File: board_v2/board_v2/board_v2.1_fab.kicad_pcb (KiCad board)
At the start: 2 copper layers, 55 x 61.5 mm, 38 parts, among them J1 Battery, J2 MOTR_SENS, J3 MOTL_SENS, J4 MOTL, J6 MOTR, SW1 SW_SPDT, U1 LD33V, U2 MPU-6050-Breakout, U3 DRV8313PWP, U5 DRV8313PWP

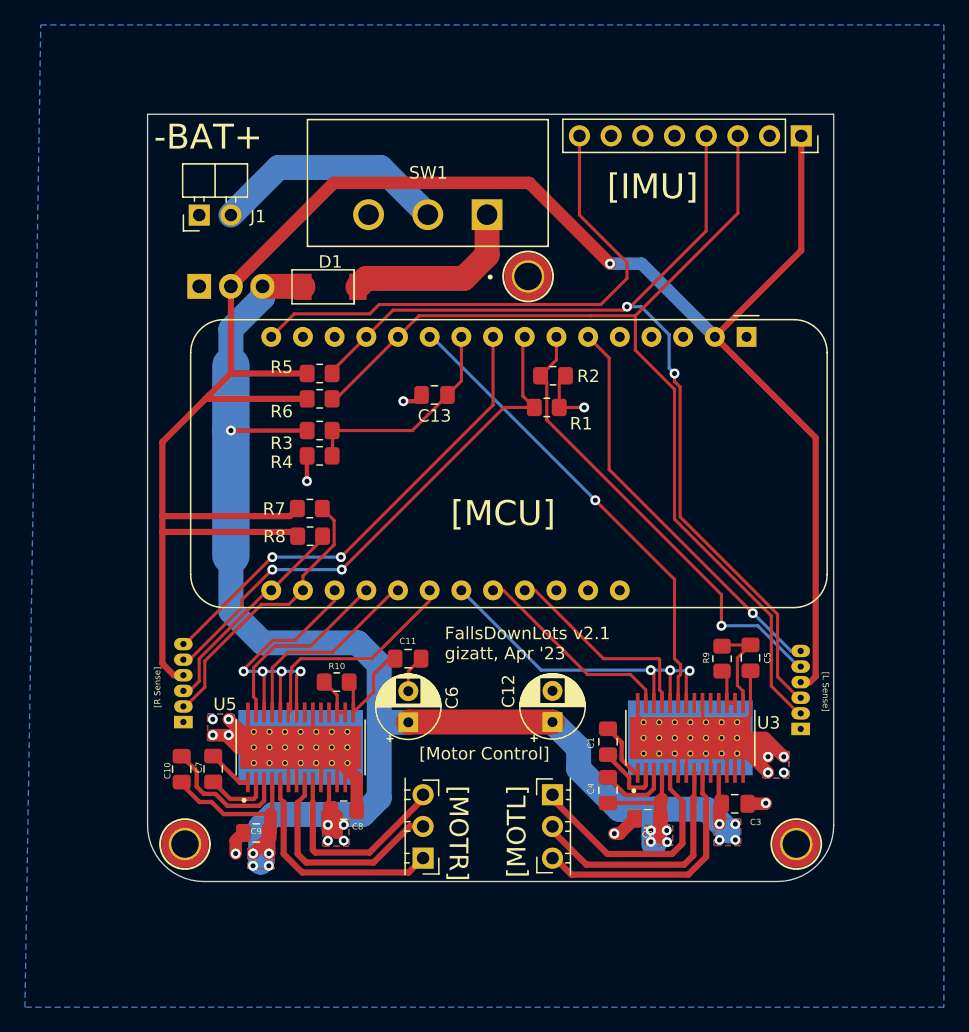
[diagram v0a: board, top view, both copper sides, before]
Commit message: Update V2 board schematics
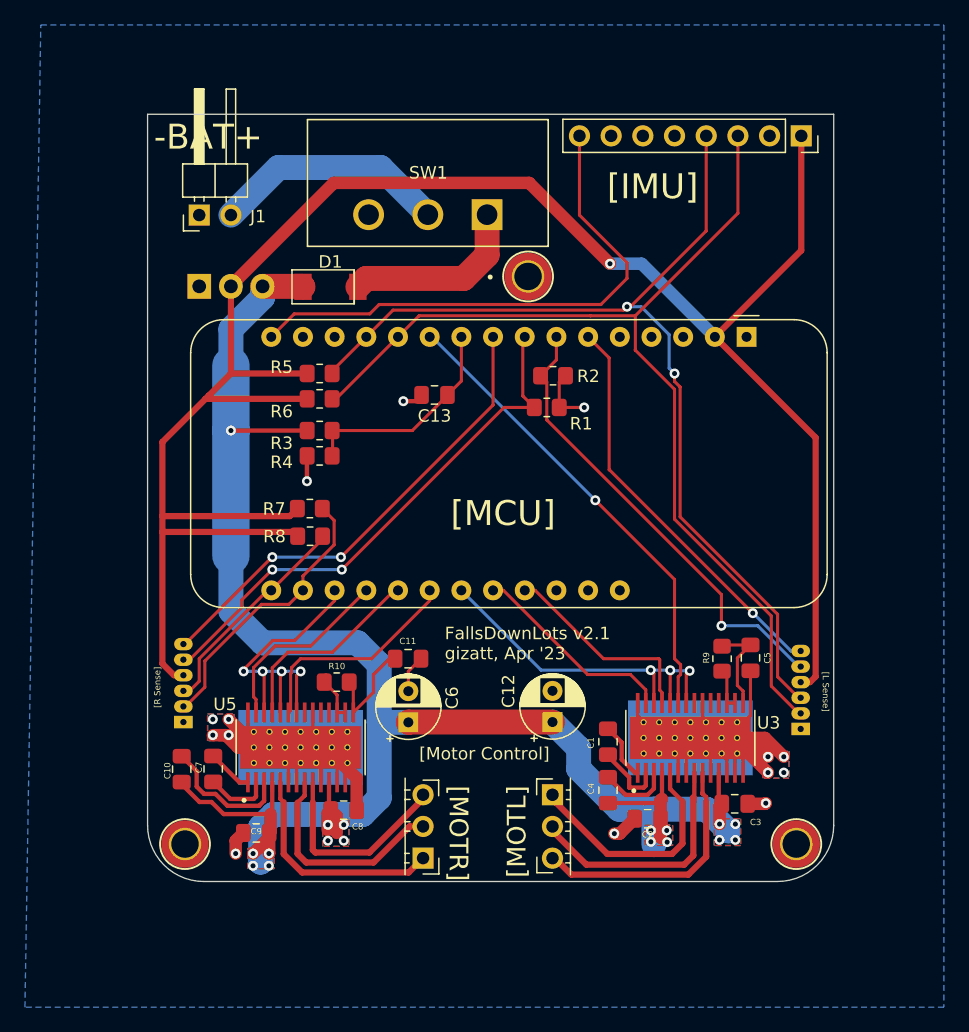
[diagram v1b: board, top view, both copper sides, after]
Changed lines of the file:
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@@
       (drillshape 0)
       (scaleselection 1)
-      (outputdirectory "v2.1_fab")
+      (outputdirectory "v2_fab")
     )
   )
@@
     (fp_line (start 4.1 -1.33) (end 1.44 -1.33)
       (stroke (width 0.12) (type solid)) (layer "F.SilkS"))
+    (fp_line (start 4.1 -0.38) (end 10.1 -0.38)
+      (stroke (width 0.12) (type solid)) (layer "F.SilkS"))
+    (fp_line (start 4.1 -0.32) (end 10.1 -0.32)
+      (stroke (width 0.12) (type solid)) (layer "F.SilkS"))
+    (fp_line (start 4.1 -0.2) (end 10.1 -0.2)
+      (stroke (width 0.12) (type solid)) (layer "F.SilkS"))
+    (fp_line (start 4.1 -0.08) (end 10.1 -0.08)
+      (stroke (width 0.12) (type solid)) (layer "F.SilkS"))
+    (fp_line (start 4.1 0.04) (end 10.1 0.04)
+      (stroke (width 0.12) (type solid)) (layer "F.SilkS"))
+    (fp_line (start 4.1 0.16) (end 10.1 0.16)
+      (stroke (width 0.12) (type solid)) (layer "F.SilkS"))
+    (fp_line (start 4.1 0.28) (end 10.1 0.28)
+      (stroke (width 0.12) (type solid)) (layer "F.SilkS"))
+    (fp_line (start 4.1 2.16) (end 10.1 2.16)
+      (stroke (width 0.12) (type solid)) (layer "F.SilkS"))
     (fp_line (start 4.1 3.87) (end 4.1 -1.33)
       (stroke (width 0.12) (type solid)) (layer "F.SilkS"))
+    (fp_line (start 10.1 -0.38) (end 10.1 0.38)
+      (stroke (width 0.12) (type solid)) (layer "F.SilkS"))
+    (fp_line (start 10.1 0.38) (end 4.1 0.38)
+      (stroke (width 0.12) (type solid)) (layer "F.SilkS"))
+    (fp_line (start 10.1 2.16) (end 10.1 2.92)
+      (stroke (width 0.12) (type solid)) (layer "F.SilkS"))
+    (fp_line (start 10.1 2.92) (end 4.1 2.92)
+      (stroke (width 0.12) (type solid)) (layer "F.SilkS"))
     (fp_line (start -1.8 -1.8) (end -1.8 4.35)
       (stroke (width 0.05) (type solid)) (layer "F.CrtYd"))
@@
     (fp_line (start 4.04 -1.27) (end 4.04 3.81)
       (stroke (width 0.1) (type solid)) (layer "F.Fab"))
+    (fp_line (start 4.04 -0.32) (end 10.04 -0.32)
+      (stroke (width 0.1) (type solid)) (layer "F.Fab"))
+    (fp_line (start 4.04 0.32) (end 10.04 0.32)
+      (stroke (width 0.1) (type solid)) (layer "F.Fab"))
+    (fp_line (start 4.04 2.22) (end 10.04 2.22)
+      (stroke (width 0.1) (type solid)) (layer "F.Fab"))
+    (fp_line (start 4.04 2.86) (end 10.04 2.86)
+      (stroke (width 0.1) (type solid)) (layer "F.Fab"))
     (fp_line (start 4.04 3.81) (end 1.5 3.81)
       (stroke (width 0.1) (type solid)) (layer "F.Fab"))
+    (fp_line (start 10.04 -0.32) (end 10.04 0.32)
+      (stroke (width 0.1) (type solid)) (layer "F.Fab"))
+    (fp_line (start 10.04 2.22) (end 10.04 2.86)
+      (stroke (width 0.1) (type solid)) (layer "F.Fab"))
     (pad "1" thru_hole rect (at 0 0 90) (size 1.7 1.7) (drill 1) (layers "*.Cu" "*.Mask")
       (net 2 "GND") (pinfunction "Pin_1") (pintype "passive"))
@@
     (fp_line (start 1 0.625) (end -1 0.625)
       (stroke (width 0.1) (type solid)) (layer "F.Fab"))
-    (pad "1" smd roundrect (at -1 0) (size 1.2 1.4) (layers "F.Cu" "F.Paste" "F.Mask") (roundrect_rratio 0.2083333333)
+    (pad "1" smd roundrect (at -1 0) (size 1.2 1.4) (layers "F.Cu" "F.Paste" "F.Mask") (roundrect_rratio 0.208333)
       (net 44 "Net-(U5-NRESET)") (pintype "passive"))
-    (pad "2" smd roundrect (at 1 0) (size 1.2 1.4) (layers "F.Cu" "F.Paste" "F.Mask") (roundrect_rratio 0.2083333333)
+    (pad "2" smd roundrect (at 1 0) (size 1.2 1.4) (layers "F.Cu" "F.Paste" "F.Mask") (roundrect_rratio 0.208333)
       (net 39 "Net-(U5-V3P3)") (pintype "passive"))
     (model "${KICAD6_3DMODEL_DIR}/Resistor_SMD.3dshapes/R_0805_2012Metric.wrl"
@@
     (fp_line (start 1 0.625) (end -1 0.625)
       (stroke (width 0.1) (type solid)) (layer "F.Fab"))
-    (pad "1" smd roundrect (at -1 0 90) (size 1.2 1.4) (layers "F.Cu" "F.Paste" "F.Mask") (roundrect_rratio 0.2083333333)
+    (pad "1" smd roundrect (at -1 0 90) (size 1.2 1.4) (layers "F.Cu" "F.Paste" "F.Mask") (roundrect_rratio 0.208333)
       (net 40 "Net-(U3-NRESET)") (pintype "passive"))
-    (pad "2" smd roundrect (at 1 0 90) (size 1.2 1.4) (layers "F.Cu" "F.Paste" "F.Mask") (roundrect_rratio 0.2083333333)
+    (pad "2" smd roundrect (at 1 0 90) (size 1.2 1.4) (layers "F.Cu" "F.Paste" "F.Mask") (roundrect_rratio 0.208333)
       (net 29 "Net-(U3-V3P3)") (pintype "passive"))
     (model "${KICAD6_3DMODEL_DIR}/Resistor_SMD.3dshapes/R_0805_2012Metric.wrl"
@@
     (fp_line (start 1 0.625) (end -1 0.625)
       (stroke (width 0.1) (type solid)) (layer "F.Fab"))
-    (pad "1" smd roundrect (at -1 0) (size 1.2 1.4) (layers "F.Cu" "F.Paste" "F.Mask") (roundrect_rratio 0.2083333333)
+    (pad "1" smd roundrect (at -1 0) (size 1.2 1.4) (layers "F.Cu" "F.Paste" "F.Mask") (roundrect_rratio 0.208333)
       (net 1 "+3V3") (pintype "passive"))
-    (pad "2" smd roundrect (at 1 0) (size 1.2 1.4) (layers "F.Cu" "F.Paste" "F.Mask") (roundrect_rratio 0.2083333333)
+    (pad "2" smd roundrect (at 1 0) (size 1.2 1.4) (layers "F.Cu" "F.Paste" "F.Mask") (roundrect_rratio 0.208333)
       (net 8 "/SDA0") (pintype "passive"))
     (model "${KICAD6_3DMODEL_DIR}/Resistor_SMD.3dshapes/R_0805_2012Metric.wrl"
@@
     (fp_line (start 1 0.625) (end -1 0.625)
       (stroke (width 0.1) (type solid)) (layer "F.Fab"))
-    (pad "1" smd roundrect (at -1 0) (size 1.2 1.4) (layers "F.Cu" "F.Paste" "F.Mask") (roundrect_rratio 0.2083333333)
+    (pad "1" smd roundrect (at -1 0) (size 1.2 1.4) (layers "F.Cu" "F.Paste" "F.Mask") (roundrect_rratio 0.208333)
       (net 1 "+3V3") (pintype "passive"))
-    (pad "2" smd roundrect (at 1 0) (size 1.2 1.4) (layers "F.Cu" "F.Paste" "F.Mask") (roundrect_rratio 0.2083333333)
+    (pad "2" smd roundrect (at 1 0) (size 1.2 1.4) (layers "F.Cu" "F.Paste" "F.Mask") (roundrect_rratio 0.208333)
       (net 9 "/SCL0") (pintype "passive"))
     (model "${KICAD6_3DMODEL_DIR}/Resistor_SMD.3dshapes/R_0805_2012Metric.wrl"
